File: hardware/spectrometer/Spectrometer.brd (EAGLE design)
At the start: 60 x 30 mm, 97 parts, among them IC501 LT1763IDE-3.3, IC502 LT1763IDE-5, U101 TLC59208FTSSOP-16, U201 ADS1255TSSOP, U202 OPA2376PDSO-8, U203 OPA350PDSO-8, U204 REF5025PDSO-8, U301 STM32F302K8U6UFQFPN32, X301 8MHz, X302 CORTEX-MDEBUG-10P, X401 632723300011THT

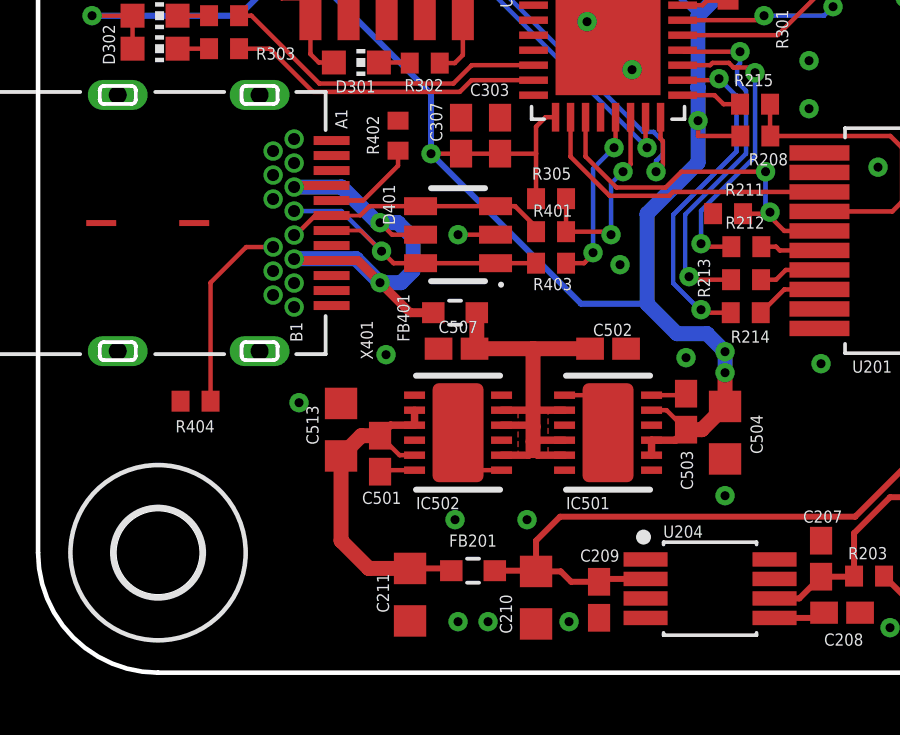
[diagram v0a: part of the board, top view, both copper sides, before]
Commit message: changed library dependencies
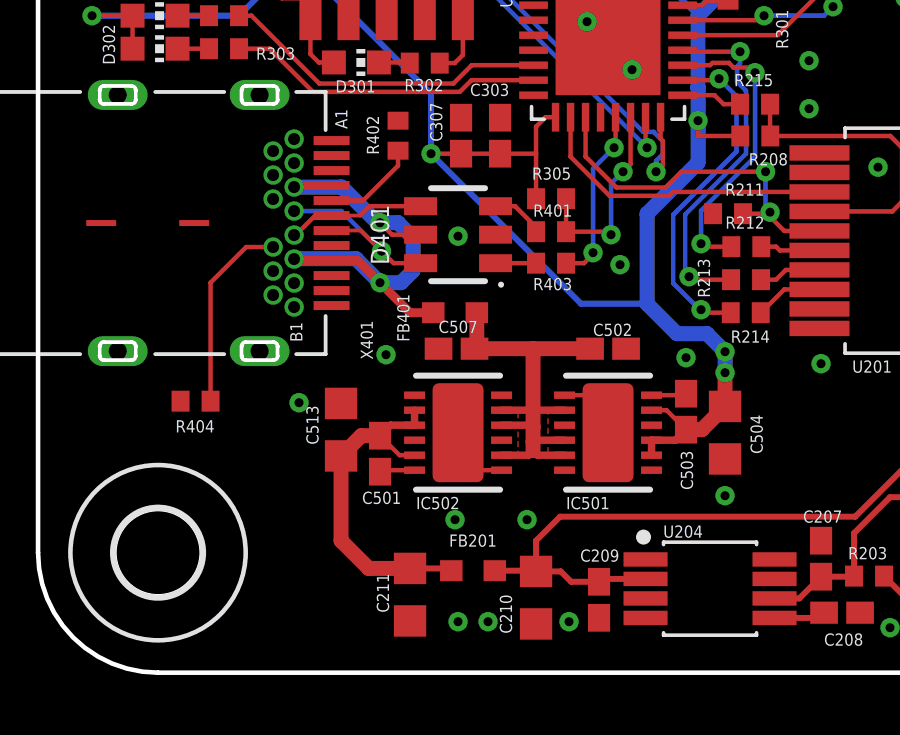
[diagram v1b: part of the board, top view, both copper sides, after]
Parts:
- D401: value 5Vdc/2pF -> 5Vdc; device EMCComponents (rev19c):WE-TVS_SOT23-6L -> Wurth_EMC Components_WE-TVS:WE-TVS_SOT23-6L
- FB201, FB401: value 240 -> 240Ohm@100MHz; device EMCComponents (rev19c):WE-CBF_0603(W=2.2) -> Wurth_EMC Components_WE-CBF:WE-CBF_0603(W=2.2)
- X302: device BMAS:CORTEX-M-CON-10P -> spectrometer:CORTEX-M-CON-10P
- turned D401 to 90 degrees
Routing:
- net USB1:DN: track 10.7 -> 8.24 mm
- net USB1:DP: track 8.98 -> 6.48 mm
- net GND: track 6.34 -> 5.09 mm
